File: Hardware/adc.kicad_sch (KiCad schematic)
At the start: 13 parts, among them U2 NAU7802SGI, X1 SG-8002CE

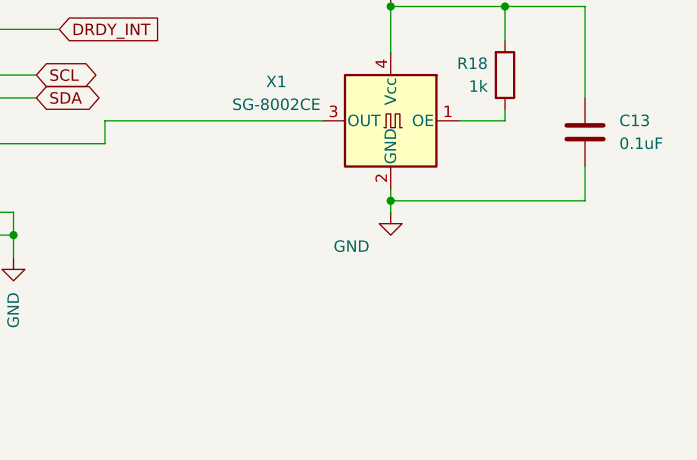
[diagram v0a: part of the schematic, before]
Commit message: added recommended crystal layout to board
Signed-off-by: lokimetasmith <lokimail@gmail.com>
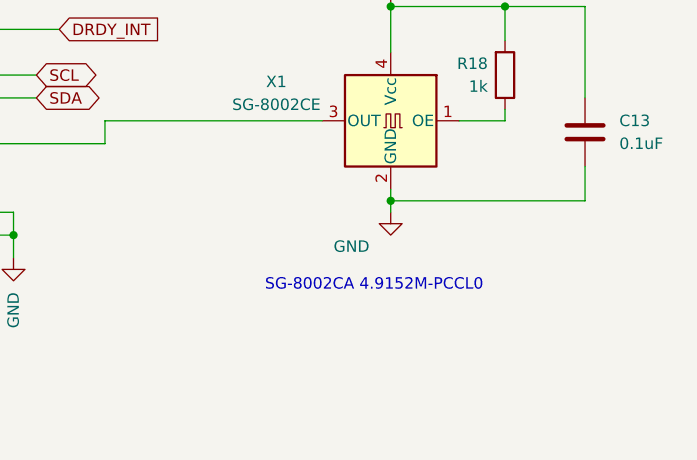
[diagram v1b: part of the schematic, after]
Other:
- note added: "SG-8002CA 4.9152M-PCCL0"
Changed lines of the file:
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@@
+    (effects (font (size 1.27 1.27)) (justify left bottom))
+  )
+  (text "SG-8002CA 4.9152M-PCCL0" (at 207.01 132.08 0)
     (effects (font (size 1.27 1.27)) (justify left bottom))
   )
